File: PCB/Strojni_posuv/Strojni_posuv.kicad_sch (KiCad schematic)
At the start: 43 parts, among them J1 Conn_01x20_Pin, J10 Button_right_A, J7 Button_left_A, J8 Button_left_B, J9 Button_right_A, SW1 SW_DPST_x2, SW2 SW_DPST_x2, SW3 SW_DPST_x2, U1 STM32F103RBTx, Y1 16MHz

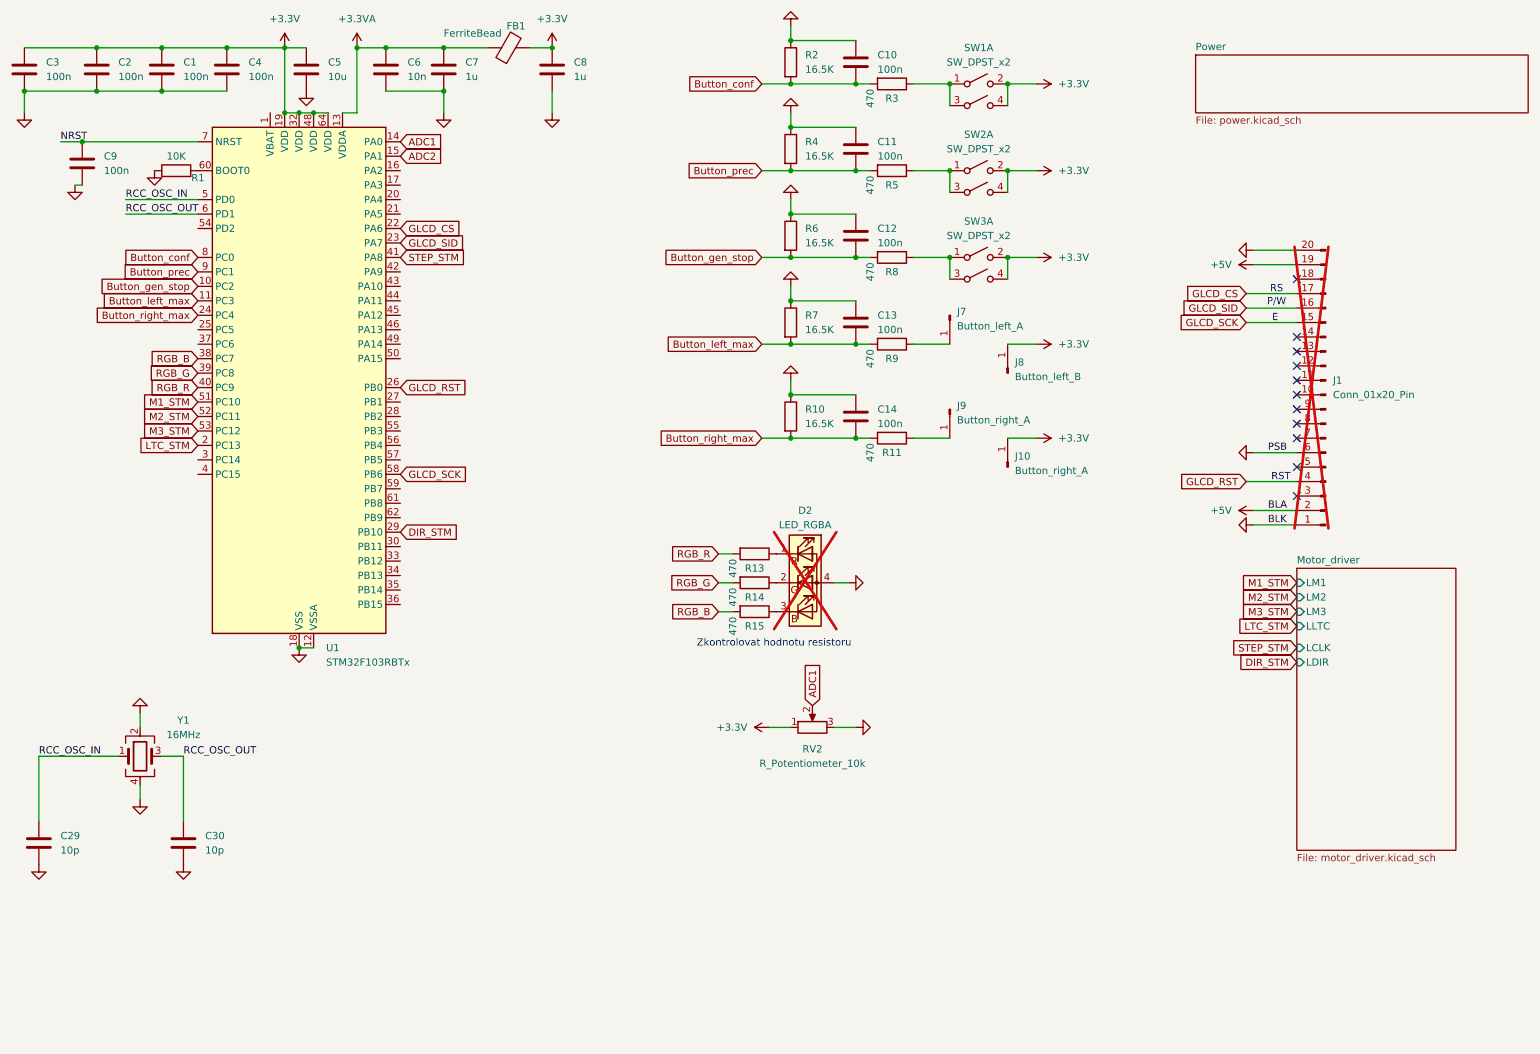
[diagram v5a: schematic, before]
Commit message: New chapter of PCB making #1
the grind continuesmkdir Useful_materials. redundant systems for 5V logic shifting. 2. rotary encoder. 3. new buttons. 4. placement of components (it is not completed)
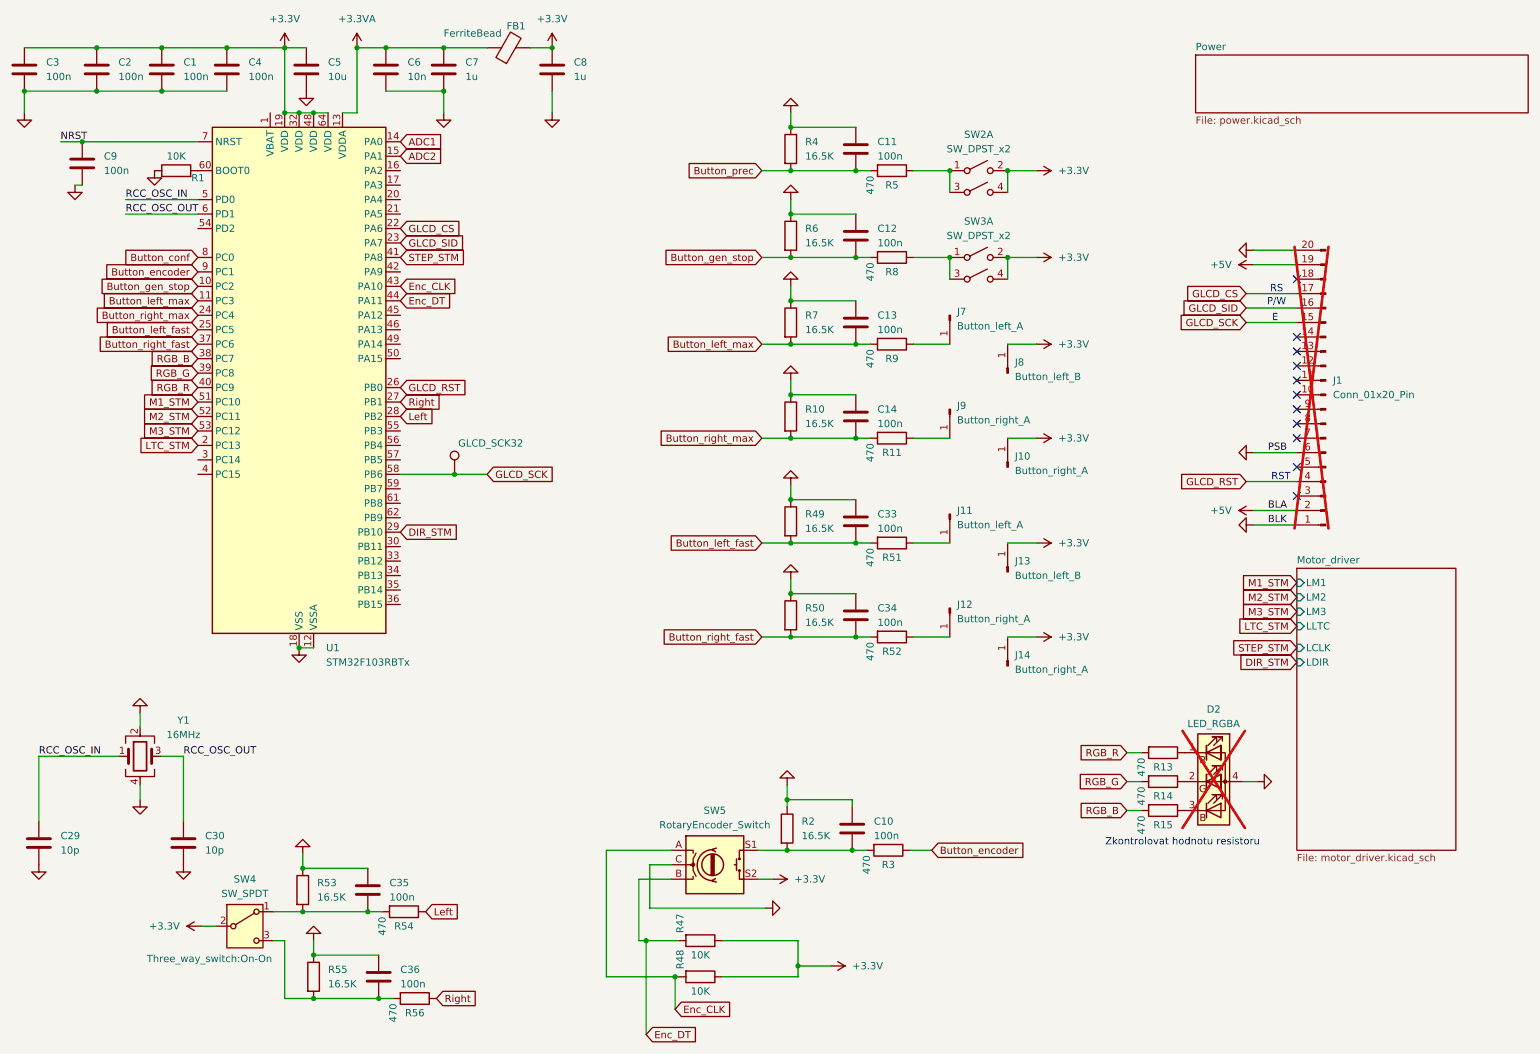
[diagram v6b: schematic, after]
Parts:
- removed RV2: R_Potentiometer_10k, Potentiometer_THT:Potentiometer_Alps_RK09K_Single_Vertical, symbol Device:R_Potentiometer
- removed SW1: SW_DPST_x2, Button_Switch_THT:SW_PUSH_6mm, symbol Switch:SW_DPST_x2
- added C33, C34, C35, C36: 100n, Capacitor_SMD:C_0603_1608Metric, symbol Device:C
- added GLCD_SCK32: ~, TestPoint:TestPoint_Pad_D1.0mm, symbol Connector:TestPoint
- added J11: Button_left_A, Connector_Pin:Pin_D1.3mm_L11.3mm_W2.8mm_Flat, symbol Connector:Conn_01x01_Pin
- added J12, J14: Button_right_A, Connector_Pin:Pin_D1.3mm_L11.3mm_W2.8mm_Flat, symbol Connector:Conn_01x01_Pin
- added J13: Button_left_B, Connector_Pin:Pin_D1.3mm_L11.3mm_W2.8mm_Flat, symbol Connector:Conn_01x01_Pin
- added R47, R48: 10K, Resistor_SMD:R_0603_1608Metric, symbol Device:R
- added R49, R50, R53, R55: 16.5K, Resistor_SMD:R_0603_1608Metric, symbol Device:R
- added R51, R52, R54, R56: 470, Resistor_SMD:R_0603_1608Metric, symbol Device:R
- added SW4: SW_SPDT, Three_way_switch:On-On, symbol Switch:SW_SPDT
- added SW5: RotaryEncoder_Switch, Encoder:Rotary_encoder_GME, symbol Device:RotaryEncoder_Switch
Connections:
- net +3.3V: now also J13.1 (Pin_1), J14.1 (Pin_1), R47.1, R48.1, SW4.2 (B), SW5.S2
- net Button_conf: no longer C10.2, R2.2, R3.2
- net Button_prec: no longer U1.9 (PC1)
- net GLCD_SCK: now also GLCD_SCK32.1
- net GND: now also C33.1, C34.1, C35.1, C36.1, R49.1, R50.1, R53.1, R55.1, SW5.C
- net Button_encoder: now reaches R3.1
- net Button_encoder: now also U1.9 (PC1)
- net Button_left_fast: now reaches U1.25 (PC5)
- net Button_left_fast: now also C33.2, R49.2, R51.2
- net Right: now reaches U1.27 (PB1)
- net Right: now also R56.1
- net Left: now reaches U1.28 (PB2)
- net Left: now also R54.1
- net Button_right_fast: now reaches U1.37 (PC6)
- net Button_right_fast: now also C34.2, R50.2, R52.2
- net Enc_CLK: now reaches U1.43 (PA10)
- net Enc_CLK: now also R48.2, SW5.A
- net Enc_DT: now reaches U1.44 (PA11)
- net Enc_DT: now also R47.2, SW5.B
- new net: C35.2, R53.2, R54.2, SW4.1 (A)
- new net: C10.2, R2.2, R3.2, SW5.S1
- new net: J11.1 (Pin_1), R51.1
- new net: C36.2, R55.2, R56.2, SW4.3 (C)
- new net: J12.1 (Pin_1), R52.1
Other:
- moved on the sheet: C10, D2, R13, R14, R15, R2, R3

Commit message: New chapter of PCB making #2
pcb placement
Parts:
- J11: value Button_left_A -> Button_left_fast_A
- J12: value Button_right_A -> Button_right_fast_A
- J13: value Button_left_B -> Button_left_fast_B
- J14: value Button_right_A -> Button_right_fast_B
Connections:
- net Left: now also C35.2, R53.2
- net Right: now also C36.2, R55.2
- net at R54.2, SW4.1 (A): no longer C35.2, R53.2
- net at R56.2, SW4.3 (C): no longer C36.2, R55.2
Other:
- moved on the sheet: C35, C36, R53, R54, R55, R56, SW4

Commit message: Revision 0
The PCB is done
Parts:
- added J15: Conn_01x06_Socket, Connector_PinSocket_2.54mm:PinSocket_1x06_P2.54mm_Vertical, symbol Connector:Conn_01x06_Socket
- U1: LCSC (none) -> C8735
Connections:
- net Button_prec is gone; now on net Button_conf: C11.2, R4.2, R5.2
- net +3.3V: now also J15.3 (Pin_3)
- net GND: now also J15.4 (Pin_4)
- net NRST: now also J15.2 (Pin_2)
- net SWDIO: now reaches U1.46 (PA13)
- net SWDIO: now also J15.5 (Pin_5)
- net SWCLK: now reaches U1.49 (PA14)
- net SWCLK: now also J15.6 (Pin_6)
- no-connect marks 11 -> 12
